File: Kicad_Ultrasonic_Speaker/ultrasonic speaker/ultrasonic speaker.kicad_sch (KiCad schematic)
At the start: 12 parts, among them J1 To_Array, J2 Conn_01x02_Female, U1 ESP32_DevKit_V1_DOIT, U2 MIC4427, U3 LM317

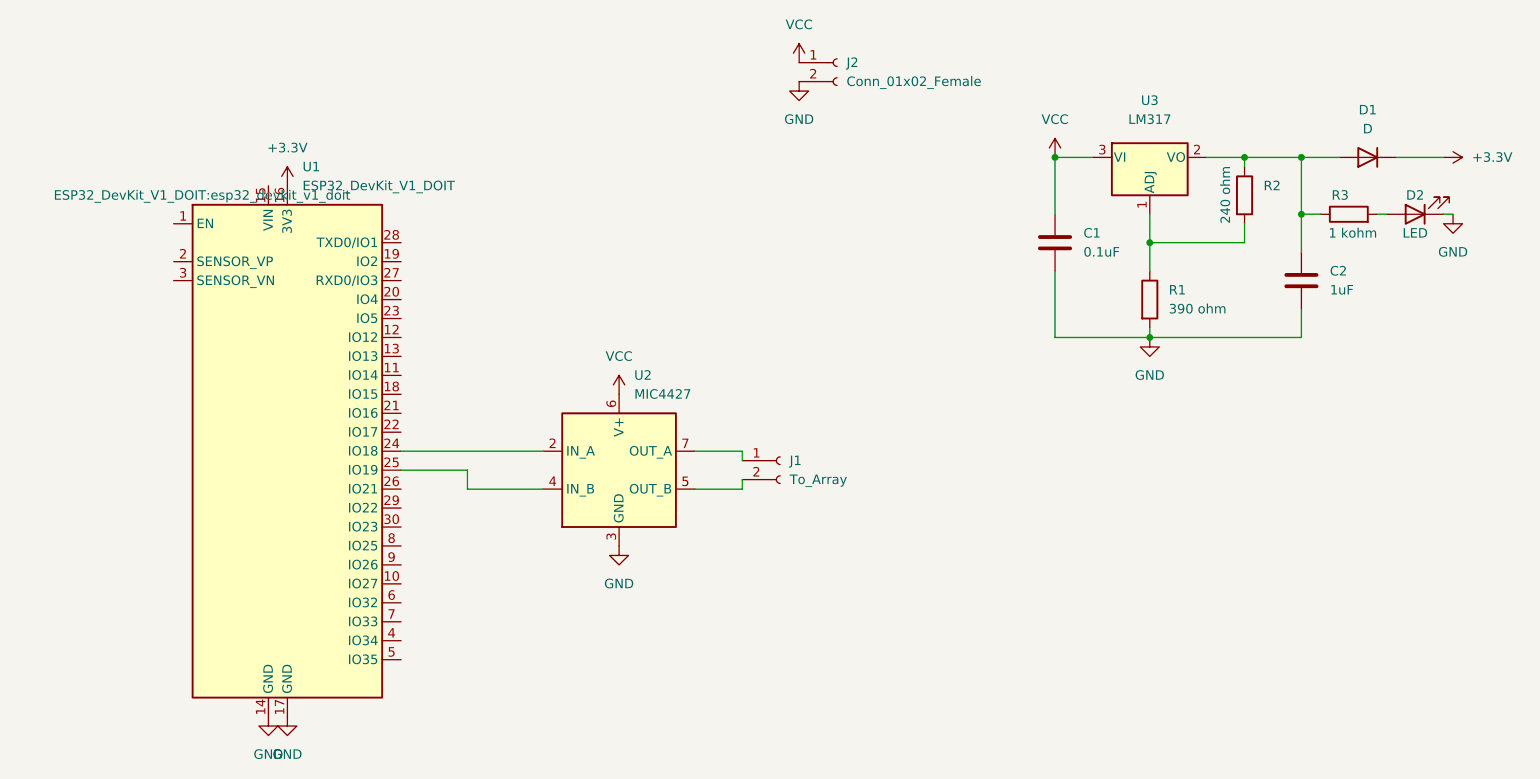
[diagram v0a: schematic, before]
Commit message: change for boost converter
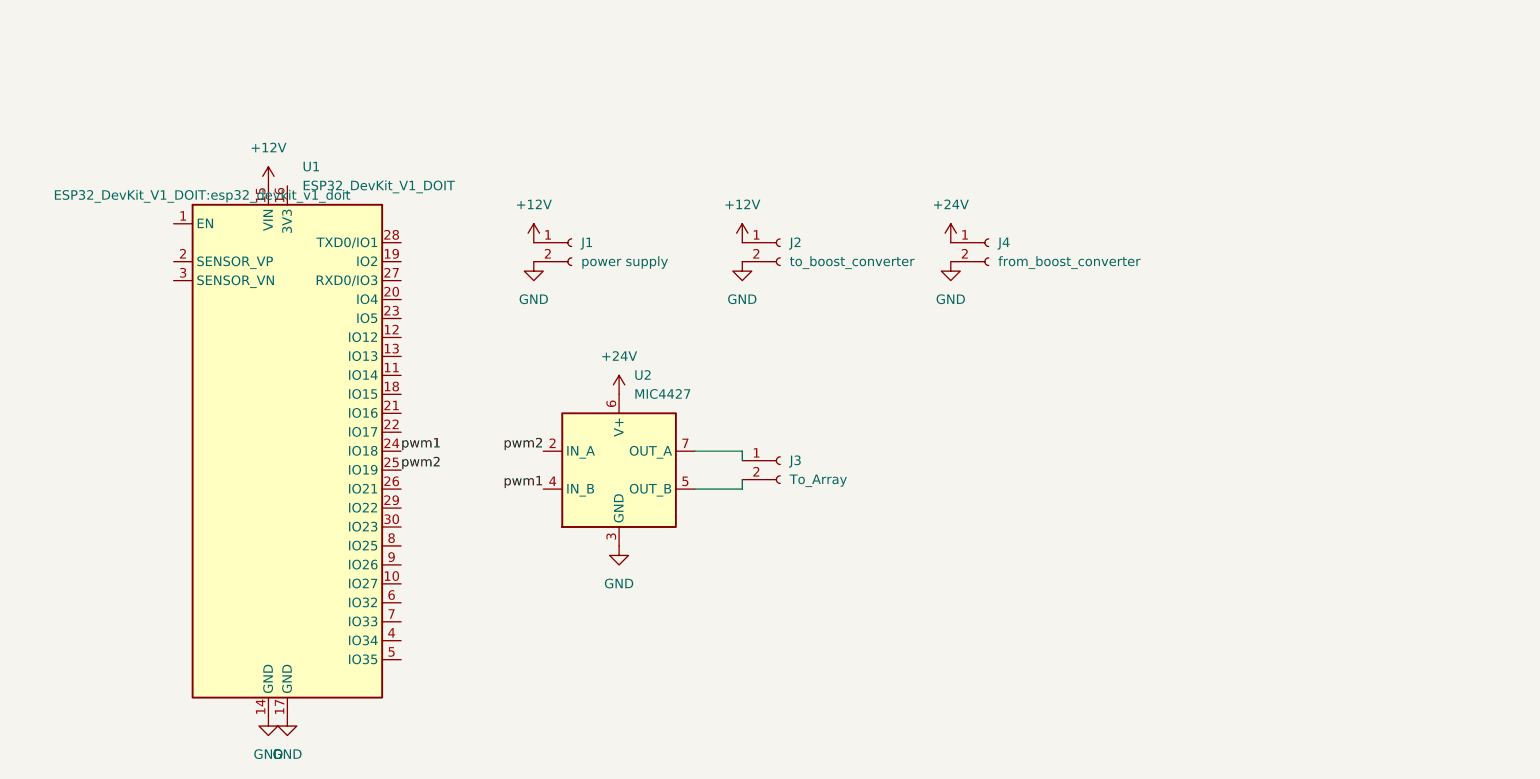
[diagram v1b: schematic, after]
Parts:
- removed C1: 0.1uF, Capacitor_SMD:C_0603_1608Metric_Pad1.08x0.95mm_HandSolder, symbol Device:C
- removed C2: 1uF, Capacitor_SMD:C_0603_1608Metric_Pad1.08x0.95mm_HandSolder, symbol Device:C
- removed D1: D, Diode_SMD:D_0603_1608Metric_Pad1.05x0.95mm_HandSolder, symbol Device:D
- removed D2: LED, LED_SMD:LED_0805_2012Metric_Pad1.15x1.40mm_HandSolder, symbol Device:LED
- removed R1: 390 ohm, Resistor_SMD:R_0603_1608Metric_Pad0.98x0.95mm_HandSolder, symbol Device:R
- removed R2: 240 ohm, Resistor_SMD:R_0603_1608Metric_Pad0.98x0.95mm_HandSolder, symbol Device:R
- removed R3: 1 kohm, Resistor_SMD:R_0603_1608Metric_Pad0.98x0.95mm_HandSolder, symbol Device:R
- removed U3: LM317, Package_TO_SOT_SMD:SOT-223-3_TabPin2, symbol Regulator_Linear:LM317_SOT-223
- added J2: to_boost_converter, librarie:TerminalBlock_Phoenix_MKDS-1,5-2_1x02_P5.00mm_Horizontal, symbol Connector:Conn_01x02_Female
- added J4: from_boost_converter, librarie:TerminalBlock_Phoenix_MKDS-1,5-2_1x02_P5.00mm_Horizontal, symbol Connector:Conn_01x02_Female
- J1: renamed from J2; value Conn_01x02_Female -> power supply; footprint TerminalBlock_TE-Connectivity:TerminalBlock_TE_282834-2_1x02_P2.54mm_Horizontal -> librarie:TerminalBlock_Phoenix_MKDS-1,5-2_1x02_P5.00mm_Horizontal
- J3: renamed from J1; footprint TerminalBlock_TE-Connectivity:TerminalBlock_TE_282834-2_1x02_P2.54mm_Horizontal -> librarie:TerminalBlock_Phoenix_MKDS-1,5-2_1x02_P5.00mm_Horizontal
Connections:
- net GND: now also J2.2 (Pin_2), J4.2 (Pin_2)
- net +12V: now reaches U1.15 (VIN)
- net +12V: now also J1.1 (Pin_1), J2.1 (Pin_1)
- net pwm1: now reaches U1.24 (IO18)
- net pwm1: now also U2.4 (IN_B); no longer U2.2 (IN_A)
- net pwm2: now reaches U1.25 (IO19)
- net pwm2: now also U2.2 (IN_A); no longer U2.4 (IN_B)
- net +3.3V: no longer names the net of U1.16 (3V3)
- net VCC renamed +24V
- net +24V: now also J4.1 (Pin_1); no longer J1.1 (Pin_1)
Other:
- moved on the sheet: J1

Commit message: simple save
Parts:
- U1: footprint ESP32_DevKit_V1_DOIT:esp32_devkit_v1_doit -> esp32_devkit_v1_doit:esp32_devkit_v1_doit
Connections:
- net pwm1: now also U2.2 (IN_A); no longer U2.4 (IN_B)
- net pwm2: now also U2.4 (IN_B); no longer U2.2 (IN_A)
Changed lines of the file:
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@@
     (stroke (width 0) (type default) (color 0 0 0 0))
   )
-  (label "pwm1" (at 110.49 91.44 180)
+  (label "pwm1" (at 110.49 86.36 180)
     (effects (font (size 1.27 1.27)) (justify right bottom))
   )
-  (label "pwm2" (at 110.49 86.36 180)
+  (label "pwm2" (at 110.49 91.44 180)
     (effects (font (size 1.27 1.27)) (justify right bottom))
   )
@@
       (effects (font (size 1.27 1.27)) (justify left))
     )
-    (property "Footprint" "ESP32_DevKit_V1_DOIT:esp32_devkit_v1_doit" (id 2) (at 64.77 52.07 0))
+    (property "Footprint" "esp32_devkit_v1_doit:esp32_devkit_v1_doit" (id 2) (at 64.77 52.07 0))
     (property "Datasheet" "https://aliexpress.com/item/32864722159.html" (id 3) (at 64.77 52.07 0)
       (effects (font (size 1.27 1.27)) hide)
@@
     )
     (path "/15ab0af0-1934-4520-be0c-d334ee577097"
-      (reference "U1") (unit 1) (value "ESP32_DevKit_V1_DOIT") (footprint "ESP32_DevKit_V1_DOIT:esp32_devkit_v1_doit")
+      (reference "U1") (unit 1) (value "ESP32_DevKit_V1_DOIT") (footprint "esp32_devkit_v1_doit:esp32_devkit_v1_doit")
     )
     (path "/dc1b93f2-98cd-47d4-85b1-5e51e238fc97"
